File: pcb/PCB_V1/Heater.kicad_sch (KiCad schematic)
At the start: 8 parts, among them J601 PTC + / switched - (3.5 mm), Q601 NTMFS5C628NLT1G, U601 UCC27524ADR

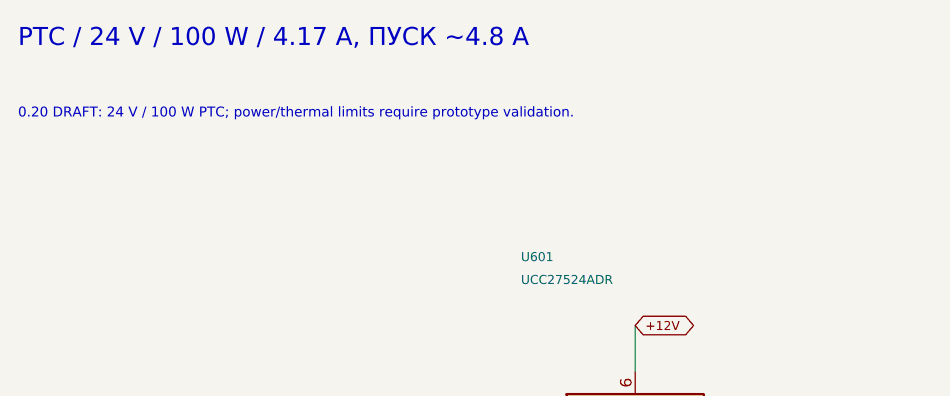
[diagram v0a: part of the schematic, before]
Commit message: pcb: use low-leakage RTC supply diode for revision 0.21
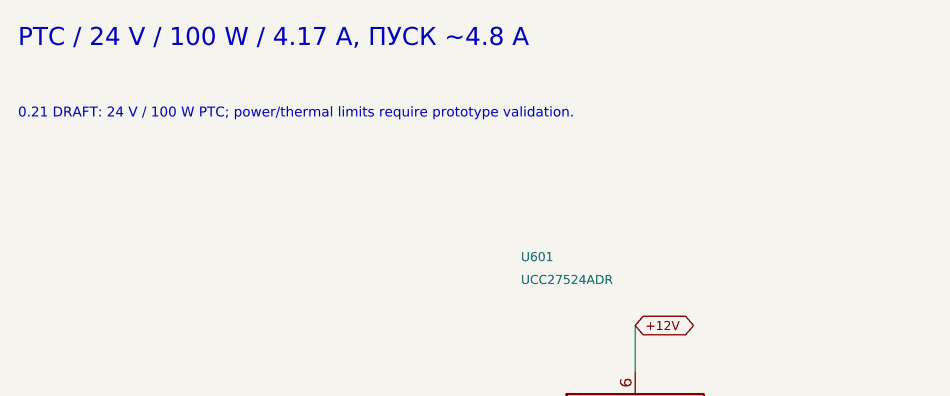
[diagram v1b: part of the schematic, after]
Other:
- note added: "0.21 DRAFT: 24 V / 100 W PTC; power/thermal limits require prototype validation."
- note removed: "0.20 DRAFT: 24 V / 100 W PTC; power/thermal limits require prototype validation."
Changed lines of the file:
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@@
 	(title_block
 		(title "05 - PTC heater switch (24 V)")
-		(date "2026-09-29")
-		(rev "0.20-DRAFT")
+		(date "2026-09-30")
+		(rev "0.21-DRAFT")
 		(company "GrowBox controller")
 		(comment 1 "Simplified prototype; unrouted; hardware qualification pending")
@@
 		)
 	)
-	(text "0.20 DRAFT: 24 V / 100 W PTC; power/thermal limits require prototype validation."
+	(text "0.21 DRAFT: 24 V / 100 W PTC; power/thermal limits require prototype validation."
 		(exclude_from_sim no)
 		(at 20.32 24.13 0)
